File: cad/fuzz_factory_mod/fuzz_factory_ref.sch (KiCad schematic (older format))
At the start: 26 parts, among them Q1601 Q_NJFET_DSG, Q902 DMMT3904W, Q903 DMMT3906W, Q904 DMMT3906W

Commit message: Continued schematic.
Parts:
- Q902, Q903, Q904: footprint Package_TO_SOT_SMD:SOT-363_SC-70-6 -> TO_SOT_Packages_SMD:SOT-363_SC-70-6
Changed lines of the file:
@@
 $Descr A4 11693 8268
 encoding utf-8
-Sheet 15 22
+Sheet 15 26
 Title ""
 Date ""
@@
 F 0 "Q903" H 4740 3954 50  0000 L CNN
 F 1 "DMMT3906W" H 4740 4045 50  0000 L CNN
-F 2 "Package_TO_SOT_SMD:SOT-363_SC-70-6" H 4750 4100 50  0001 C CNN
+F 2 "TO_SOT_Packages_SMD:SOT-363_SC-70-6" H 4750 4100 50  0001 C CNN
 F 3 "http://www.onsemi.com/pub_link/Collateral/BC856BDW1T1-D.PDF" H 4550 4000 50  0001 C CNN
 	2    4550 4000
@@
 F 0 "Q904" H 5340 4254 50  0000 L CNN
 F 1 "DMMT3906W" H 5340 4345 50  0000 L CNN
-F 2 "Package_TO_SOT_SMD:SOT-363_SC-70-6" H 5350 4400 50  0001 C CNN
+F 2 "TO_SOT_Packages_SMD:SOT-363_SC-70-6" H 5350 4400 50  0001 C CNN
 F 3 "http://www.onsemi.com/pub_link/Collateral/BC856BDW1T1-D.PDF" H 5150 4300 50  0001 C CNN
 	2    5150 4300
@@
 F 0 "Q902" H 3840 4546 50  0000 L CNN
 F 1 "DMMT3904W" H 3840 4455 50  0000 L CNN
-F 2 "Package_TO_SOT_SMD:SOT-363_SC-70-6" H 3850 4600 50  0001 C CNN
+F 2 "TO_SOT_Packages_SMD:SOT-363_SC-70-6" H 3850 4600 50  0001 C CNN
 F 3 "http://www.onsemi.com/pub_link/Collateral/BC846BDW1T1-D.PDF" H 3650 4500 50  0001 C CNN
 	2    3650 4500

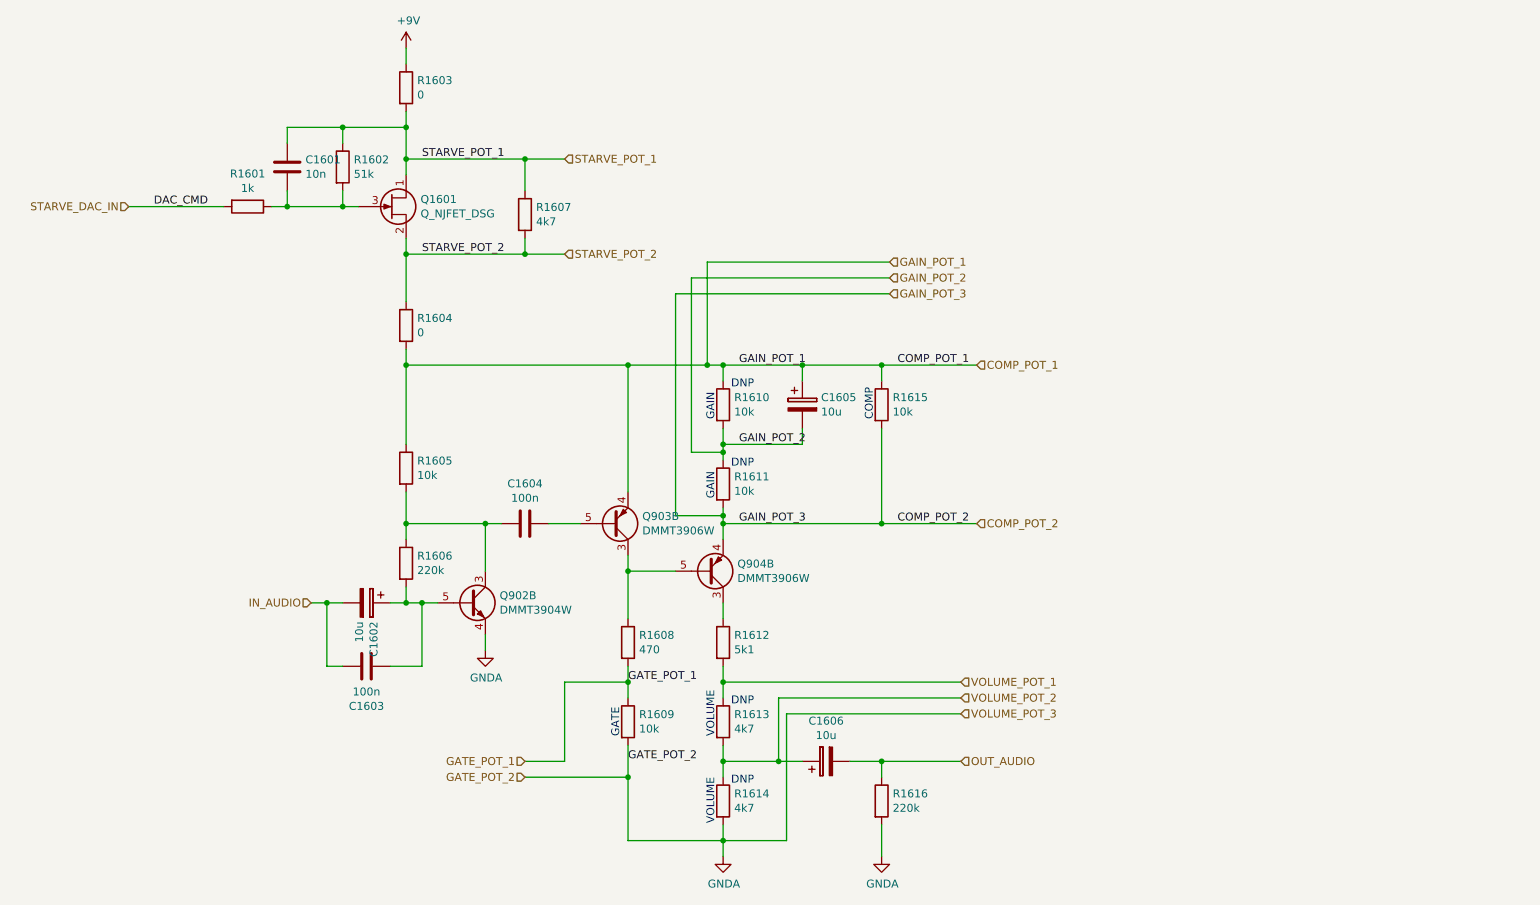
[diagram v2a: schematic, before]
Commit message: Continued schematic.
Continued component placement.
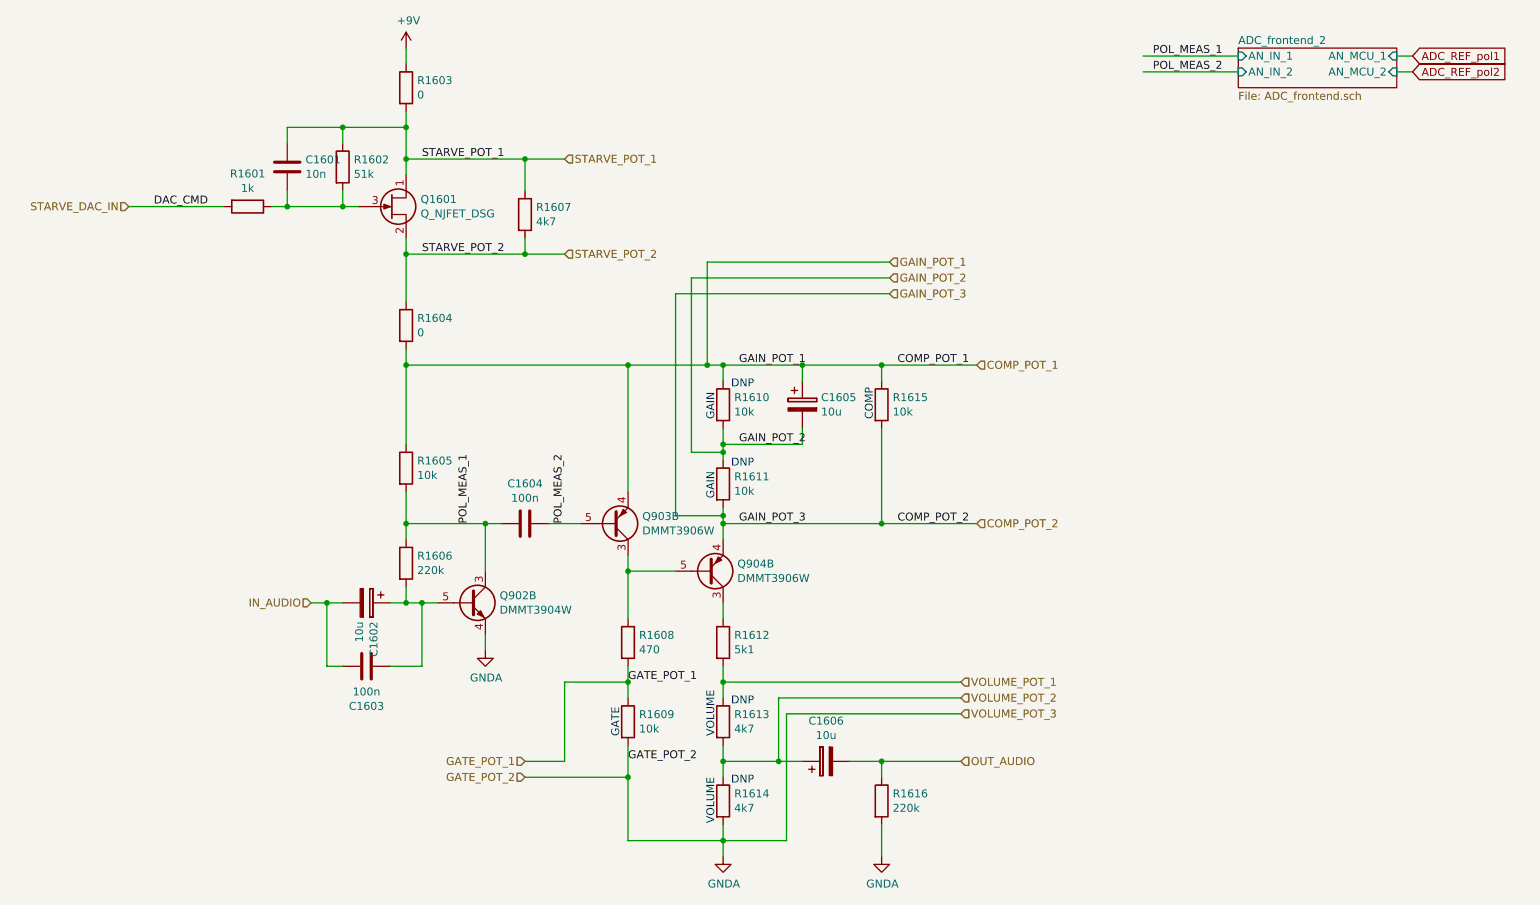
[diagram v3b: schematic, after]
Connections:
- net POL_MEAS_1: now reaches C1604.2, Q902.3 (C2), R1605.2, R1606.1
- net POL_MEAS_2: now reaches C1604.1, Q903.5 (B2)
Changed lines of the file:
@@
 $Descr A4 11693 8268
 encoding utf-8
-Sheet 15 30
+Sheet 23 30
 Title ""
 Date ""
@@
 Wire Wire Line
 	3350 4500 3450 4500
+$Sheet
+S 8500 1000 1000 250
+U 5ED2AE35
+F0 "ADC_frontend_2" 50
+F1 "ADC_frontend.sch" 50
+F2 "AN_IN_1" I L 8500 1050 50
+F3 "AN_MCU_1" I R 9500 1050 50
+F4 "AN_IN_2" I L 8500 1150 50
+F5 "AN_MCU_2" I R 9500 1150 50
+$EndSheet
+Text Label 3650 4000 1    50   ~ 0
+POL_MEAS_1
+Text Label 8400 1050 2    50   ~ 0
+POL_MEAS_1
+Text Label 8400 1150 2    50   ~ 0
+POL_MEAS_2
+Text Label 4250 4000 1    50   ~ 0
+POL_MEAS_2
+Wire Wire Line
+	8500 1050 7900 1050
+Wire Wire Line
+	8500 1150 7900 1150
+Text GLabel 9600 1050 2    50   Input ~ 0
+ADC_REF_pol1
+Text GLabel 9600 1150 2    50   Input ~ 0
+ADC_REF_pol2
+Wire Wire Line
+	9600 1050 9500 1050
+Wire Wire Line
+	9500 1150 9600 1150
 $EndSCHEMATC
